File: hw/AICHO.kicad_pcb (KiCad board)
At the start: 2 copper layers, 100 x 100 mm, 66 parts, among them J1 Conn_01x06, J101 Conn_01x03, J102 Conn_01x02, J103 Conn_01x02, J104 Conn_01x02, J2 Conn_01x02, J201 Conn_01x03, J202 Conn_01x02, J203 Conn_01x02, J204 Conn_01x02, J3 USB_A, J301 Conn_01x03, J302 Conn_01x02, J303 Conn_01x02, J304 Conn_01x02, J4 AudioJack3_SwitchTR, J401 Conn_01x03, J402 Conn_01x02, J403 Conn_01x02, J404 Conn_01x02, J5 Speaker, Q1 Si2302, Q10 Si2302, Q11 Si2302, Q12 Si2302, Q2 Si2302, Q3 Si2302, Q4 Si2302, Q5 Si2302, Q6 Si2302, Q7 Si2302, Q8 Si2302, Q9 Si2302, U1 RP2040, U2 W25Q128JVPIQ, U3 SPX3819M5-L-3-3, U4 USBLC6-2SC6, U5 MAX98357AETE+, Y1 12MHz

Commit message: 🚧 More layout
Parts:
- removed the C8 at (39.8, 90.6)
- added D1: Pink, LED_SMD:LED_0603_1608Metric, F.Cu at (78.8, 45.7)
- added D2: Pink, LED_SMD:LED_0603_1608Metric, F.Cu at (77.2, 45.7)
- added R7: 7.5k, Resistor_SMD:R_0603_1608Metric, F.Cu at (78.8, 42.7)
- added R8: 7.5k, Resistor_SMD:R_0603_1608Metric, F.Cu at (77.2, 42.7)
- C1, C2, C3, C4, C5, C6, C7: footprint Capacitor_SMD:C_0603_1608Metric -> Capacitor_SMD:C_0402_1005Metric
- C10: renamed from C11; footprint Capacitor_SMD:C_0603_1608Metric -> Capacitor_SMD:C_0402_1005Metric
- C11: renamed from C12; footprint Capacitor_SMD:C_0603_1608Metric -> Capacitor_SMD:C_0402_1005Metric
- C12: renamed from C13; footprint Capacitor_SMD:C_0603_1608Metric -> Capacitor_SMD:C_0402_1005Metric
- C13: renamed from C14; footprint Capacitor_SMD:C_0603_1608Metric -> Capacitor_SMD:C_0402_1005Metric
- C14: renamed from C15; footprint Capacitor_SMD:C_0603_1608Metric -> Capacitor_SMD:C_0402_1005Metric
- C18: renamed from C19; footprint Capacitor_SMD:C_0603_1608Metric -> Capacitor_SMD:C_0402_1005Metric
- C8: renamed from C9; footprint Capacitor_SMD:C_0603_1608Metric -> Capacitor_SMD:C_0402_1005Metric
- C9: renamed from C10; footprint Capacitor_SMD:C_0603_1608Metric -> Capacitor_SMD:C_0402_1005Metric
- moved C4 65.4 mm to (78.6, 48.7), turned to 90 degrees
- moved C5 64.7 mm to (74.4, 48.7), turned to 90 degrees
- moved C6 64.6 mm to (72.2, 49.8), turned to 180 degrees
- moved C3 64.3 mm to (83.0, 52.0)
- moved C7 63.5 mm to (72.1, 53.6), turned to 180 degrees
- moved C9 60.5 mm to (83.0, 53.2)
- moved C11 58.5 mm to (72.2, 51.9), turned to 180 degrees
- moved C2 54.4 mm to (78.6, 59.6), turned to -90 degrees
- moved C10 54.3 mm to (72.1, 54.5), turned to 180 degrees
- moved C8 53.2 mm to (72.1, 50.9), turned to 180 degrees
- moved C1 49.8 mm to (74.9, 59.8), turned to -90 degrees
- moved R3 31.4 mm to (69.3, 52.0)
- moved R2 28.9 mm to (69.3, 53.5)
- moved L1 25.6 mm to (41.7, 49.0)
- moved J102 24.8 mm to (38.0, 77.2)
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- renumbered C16 to C15, C17 to C16, C18 to C17
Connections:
- C13 pad 2: Net-(C14-Pad2) -> Net-(C13-Pad2)
- R1 pad 1: Net-(C14-Pad2) -> Net-(C13-Pad2)
- U1 pad 11: unconnected-(U1-GPIO8-Pad11) -> /ORG2_PUMP_DRAIN
- U1 pad 15: unconnected-(U1-GPIO12-Pad15) -> /ORG4_SOLENOID
- U1 pad 16: /ORG4_SOLENOID -> /ORG4_PUMP_INFLATE
- U1 pad 17: /ORG4_PUMP_INFLATE -> /ORG4_PUMP_DRAIN
- U1 pad 18: /ORG4_PUMP_DRAIN -> unconnected-(U1-GPIO15-Pad18)
- U1 pad 3: /ORG1_SOLENOID -> unconnected-(U1-GPIO1-Pad3)
- U1 pad 34: unconnected-(U1-GPIO22-Pad34) -> /ACT1
- U1 pad 35: unconnected-(U1-GPIO23-Pad35) -> /ACT2
- U1 pad 4: /ORG1_PUMP_INFLATE -> unconnected-(U1-GPIO2-Pad4)
- U1 pad 5: /ORG1_PUMP_DRAIN -> /ORG1_SOLENOID
- U1 pad 6: unconnected-(U1-GPIO4-Pad6) -> /ORG1_PUMP_INFLATE
- U1 pad 7: /ORG2_SOLENOID -> /ORG1_PUMP_DRAIN
- U1 pad 8: /ORG2_PUMP_INFLATE -> /ORG2_SOLENOID
- U1 pad 9: /ORG2_PUMP_DRAIN -> /ORG2_PUMP_INFLATE
- U4 pad 1: /USB_D- -> /USB_D+
- U4 pad 3: /USB_D+ -> /USB_D-
- U4 pad 4: /USB_RAW_D+ -> /USB_RAW_D-
- U4 pad 6: /USB_RAW_D- -> /USB_RAW_D+
- Y1 pad 1: Net-(U1-XIN) -> Net-(C13-Pad2)
- Y1 pad 3: Net-(C14-Pad2) -> Net-(U1-XIN)

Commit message: 🚧 More layout?
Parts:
- added H1: MountingHole_Pad, MountingHole:MountingHole_2.5mm_Pad_Via, F.Cu at (34.0, 34.0)
- added H2: MountingHole_Pad, MountingHole:MountingHole_2.5mm_Pad_Via, F.Cu at (34.0, 84.0)
- added H3: MountingHole_Pad, MountingHole:MountingHole_2.5mm_Pad_Via, F.Cu at (126.0, 84.0)
- added H4: MountingHole_Pad, MountingHole:MountingHole_2.5mm_Pad_Via, F.Cu at (126.0, 34.0)
- D2: value Pink -> Violet
- moved J4 92.5 mm to (34.5, 72.3), turned to -90 degrees
- moved J5 79.5 mm to (49.1, 76.8), turned to -90 degrees
- moved J404 76.8 mm to (59.0, 33.2), turned to 0 degrees
- moved J101 72.0 mm to (119.1, 71.3), turned to 90 degrees
- moved Q12 70.0 mm to (59.0, 40.0), turned to 90 degrees
- moved J403 67.4 mm to (65.0, 33.2), turned to 0 degrees
- moved U5 63.8 mm to (48.0, 68.6), turned to 180 degrees
- moved C18 63.3 mm to (47.8, 65.2), turned to 0 degrees
- moved C17 63.2 mm to (47.8, 63.5), turned to 0 degrees
- moved J201 60.7 mm to (119.1, 63.3), turned to 90 degrees
- moved Q11 59.4 mm to (65.0, 40.0), turned to 90 degrees
- moved J402 58.8 mm to (71.0, 33.2), turned to 0 degrees
- moved R6 57.3 mm to (51.1, 67.7), turned to 90 degrees
- moved J301 49.6 mm to (119.1, 55.3), turned to 90 degrees
- moved Q10 49.4 mm to (71.0, 40.0), turned to 90 degrees
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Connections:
- U1 pad 11: /ORG2_PUMP_DRAIN -> /ORG2_SOLENOID
- U1 pad 12: /ORG3_SOLENOID -> /ORG2_PUMP_INFLATE
- U1 pad 13: /ORG3_PUMP_INFLATE -> /ORG2_PUMP_DRAIN
- U1 pad 14: /ORG3_PUMP_DRAIN -> /ORG1_LED
- U1 pad 15: /ORG4_SOLENOID -> /ORG2_LED
- U1 pad 16: /ORG4_PUMP_INFLATE -> /ORG3_LED
- U1 pad 17: /ORG4_PUMP_DRAIN -> /ORG4_LED
- U1 pad 29: /I2S_CK -> /ORG3_SOLENOID
- U1 pad 30: /I2S_WS -> /ORG3_PUMP_INFLATE
- U1 pad 31: /I2S_SD -> /ORG3_PUMP_DRAIN
- U1 pad 38: /ORG4_LED -> unconnected-(U1-GPIO26_ADC0-Pad38)
- U1 pad 39: /ORG3_LED -> /ORG4_SOLENOID
- U1 pad 4: unconnected-(U1-GPIO2-Pad4) -> /I2S_SD
- U1 pad 40: /ORG2_LED -> /ORG4_PUMP_INFLATE
- U1 pad 41: /ORG1_LED -> /ORG4_PUMP_DRAIN
- U1 pad 5: /ORG1_SOLENOID -> /I2S_CK
- U1 pad 6: /ORG1_PUMP_INFLATE -> /I2S_WS
- U1 pad 7: /ORG1_PUMP_DRAIN -> /ORG1_SOLENOID
- U1 pad 8: /ORG2_SOLENOID -> /ORG1_PUMP_INFLATE
- U1 pad 9: /ORG2_PUMP_INFLATE -> /ORG1_PUMP_DRAIN
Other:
- board size 100 x 100 mm -> 100 x 58 mm

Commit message: Finish layout and routing
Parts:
- C12, C13: value 22p -> 27p
- moved C12 6.12 mm to (85.8, 55.6), turned to 180 degrees
- moved C13 5.90 mm to (86.3, 61.3), turned to 0 degrees
- moved C3 1.28 mm to (83.0, 56.3)
- moved C9 0.87 mm to (83.1, 55.4)
- moved U2 0.78 mm to (66.1, 61.7)
- moved C10 0.71 mm to (71.5, 57.8)
- moved R5 0.50 mm to (72.1, 65.6)
- moved C1 0.48 mm to (74.9, 62.4)
- moved C14 0.41 mm to (62.6, 59.8)
- moved C17 0.40 mm to (47.8, 64.0)
- moved J201 0.27 mm to (119.1, 63.0)
- moved J301 0.27 mm to (119.1, 55.0)
- moved J401 0.27 mm to (119.1, 47.0)
- moved J101 0.27 mm to (119.1, 71.0)
- moved C2 0.26 mm to (78.6, 62.3)
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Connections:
- C17 pad 2: Net-(C17-Pad2) -> GND
- C18 pad 2: Net-(C17-Pad2) -> GND
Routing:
- net +5V: track 0.00 -> 269.7 mm
- net +3V3: track 0.00 -> 135.0 mm, vias 0 -> 4
- net GND: track 0.00 -> 54.2 mm, vias 0 -> 46
- net /ORG4_LED: track 0.00 -> 48.4 mm
- net /ORG1_LED: track 0.00 -> 46.3 mm
- net /ORG3_LED: track 0.00 -> 46.1 mm
- net /ORG2_LED: track 0.00 -> 43.2 mm
- net /SWCLK: track 0.00 -> 39.6 mm
- net /SWDIO: track 0.00 -> 37.5 mm
- net /I2S_WS: track 0.00 -> 36.3 mm
- net /UART_TX: track 0.00 -> 35.0 mm
- net /I2S_CK: track 0.00 -> 34.0 mm
- net /UART_RX: track 0.00 -> 32.9 mm
- net /I2S_SD: track 0.00 -> 32.6 mm
- net /ORG2_PUMP_DRAIN: track 0.00 -> 32.2 mm
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- added copper zone on B.Cu, net GND
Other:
- outline, holes or cut-outs redrawn

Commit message: More routing (is this perfectionism??)
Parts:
- added C17: 100n, Capacitor_SMD:C_0402_1005Metric, F.Cu at (42.3, 53.6)
- added J22: Conn_01x02, Connector_PinHeader_2.54mm:PinHeader_1x02_P2.54mm_Vertical, F.Cu at (45.8, 33.6)
- moved J1 2.12 mm to (108.5, 34.9)
- renumbered C17 to C18, C18 to C19, J2 to J21
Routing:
- net +5V: track 269.7 -> 96.3 mm
- net +3V3: track 135.0 -> 119.5 mm
- net /SWDIO: track 37.5 -> 35.4 mm
- net /UART_RX: track 32.9 -> 30.7 mm
- net /UART_TX: track 35.0 -> 32.9 mm
- net /SWCLK: track 39.6 -> 37.5 mm
- net GND: track 54.2 -> 54.7 mm, vias 46 -> 62
- added copper zone on F.Cu, net +3V3
- added copper zone on B.Cu, net +5V
- added copper zone on F.Cu, net +5V

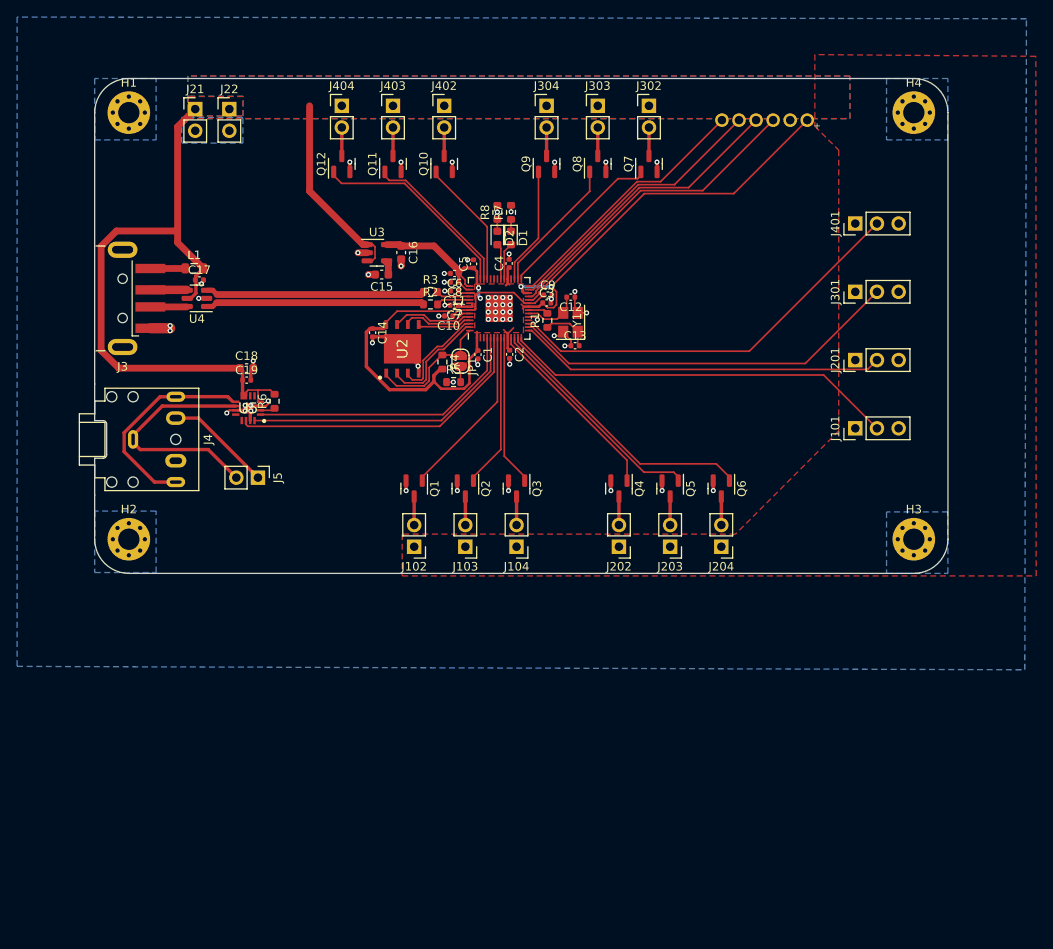
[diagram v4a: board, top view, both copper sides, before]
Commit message: Place silkscreen text
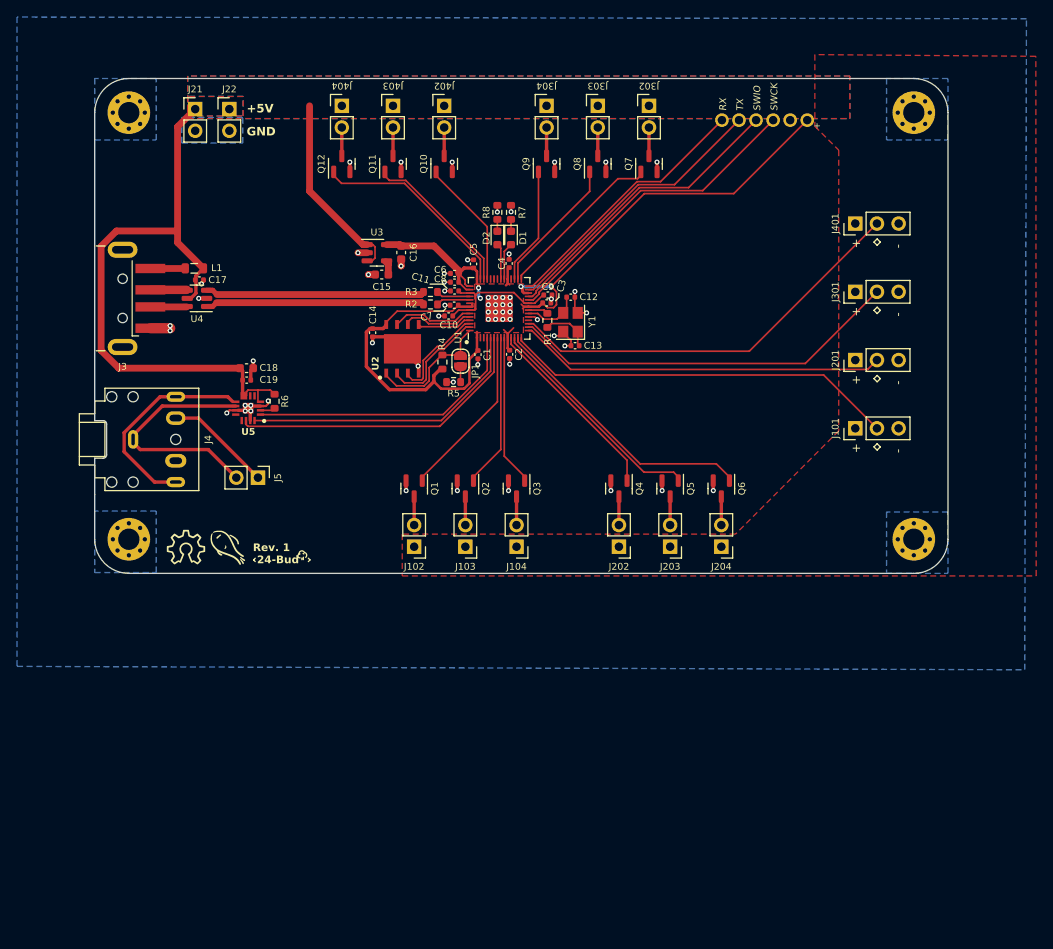
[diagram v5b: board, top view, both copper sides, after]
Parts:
- added G***: LOGO, LOGO, F.Cu at (45.7, 85.1)
- added G***: LOGO, LOGO, F.Cu at (40.7, 84.9)
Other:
- board text added: "+"
- board text added: "+5V"
- board text added: "-"
- board text added: "24-Bud"
- board text added: "GND"
- board text added: "RX"
- board text added: "Rev. 1"
- board text added: "SWCK"
- board text added: "SWIO"
- board text added: "TX"
